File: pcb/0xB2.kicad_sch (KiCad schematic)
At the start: 40 parts, among them J1 USB_C_Receptacle_USB2.0, J2 Conn_01x12, J3 Conn_01x05, J4 Conn_01x12, J5 Conn_01x01, SW1 SW_Push, SW2 SW_Push, U1 RP2040, U2 W25Q32JVZP, U3 XC6210B332MR-G, Y1 Crystal_GND24

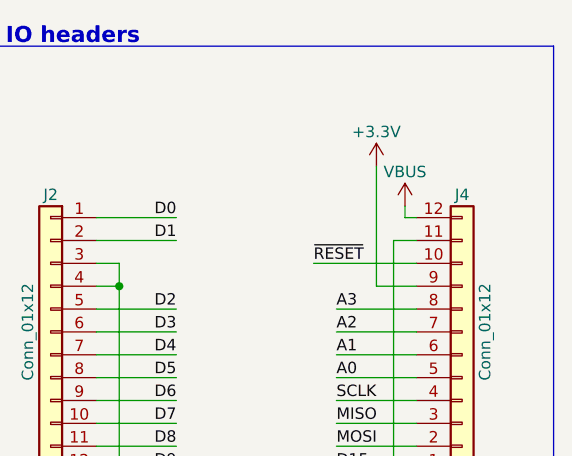
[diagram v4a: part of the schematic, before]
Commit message: Break out 5V instead of VBUS + routing update
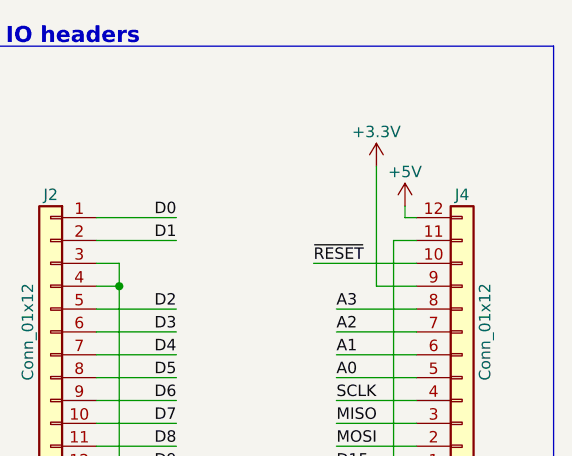
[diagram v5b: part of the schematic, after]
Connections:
- net +5V: now also J4.12 (Pin_12)
- net VBUS: no longer J4.12 (Pin_12)
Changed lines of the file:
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@@
+    (pin "1")
+  )
+  (symbol (lib_id "power:+5V") (at 262.89 38.1 0) (unit 1)
+    (in_bom yes) (on_board yes)
+    (property "Reference" "#PWR?" (id 0) (at 262.89 41.91 0)
+      (effects (font (size 1.27 1.27)) hide)
+    )
+    (property "Value" "+5V" (id 1) (at 262.89 34.29 0))
+    (property "Footprint" "" (id 2) (at 262.89 38.1 0)
+      (effects (font (size 1.27 1.27)) hide)
+    )
+    (property "Datasheet" "" (id 3) (at 262.89 38.1 0)
+      (effects (font (size 1.27 1.27)) hide)
+    )
     (pin "1")
   )
@@
     (pin "1")
   )
-  (symbol (lib_id "power:VBUS") (at 262.89 38.1 0) (unit 1)
-    (in_bom yes) (on_board yes)
-    (property "Reference" "#PWR031" (id 0) (at 262.89 41.91 0)
-      (effects (font (size 1.27 1.27)) hide)
-    )
-    (property "Value" "VBUS" (id 1) (at 262.89 34.29 0))
-    (property "Footprint" "" (id 2) (at 262.89 38.1 0)
-      (effects (font (size 1.27 1.27)) hide)
-    )
-    (property "Datasheet" "" (id 3) (at 262.89 38.1 0)
-      (effects (font (size 1.27 1.27)) hide)
-    )
-    (pin "1")
-  )
   (symbol (lib_id "Device:Polyfuse") (at 59.69 36.83 90) (unit 1)
     (in_bom yes) (on_board yes)
@@
       (reference "#PWR030") (unit 1) (value "GND") (footprint "")
     )
-    (path "/ce7cdfc2-6554-4575-a356-645785e89b5b"
-      (reference "#PWR031") (unit 1) (value "VBUS") (footprint "")
-    )
     (path "/da1644f7-6b59-4f28-b4bd-963f2f055bce"
       (reference "#PWR0101") (unit 1) (value "GND") (footprint "")
@@
       (reference "#PWR0102") (unit 1) (value "VBUS") (footprint "")
     )
+    (path "/0f2f533c-6efa-4396-afac-bd28ecf14786"
+      (reference "#PWR?") (unit 1) (value "+5V") (footprint "")
+    )
     (path "/4a21e78b-0ab0-4b88-8132-9b174e045719"

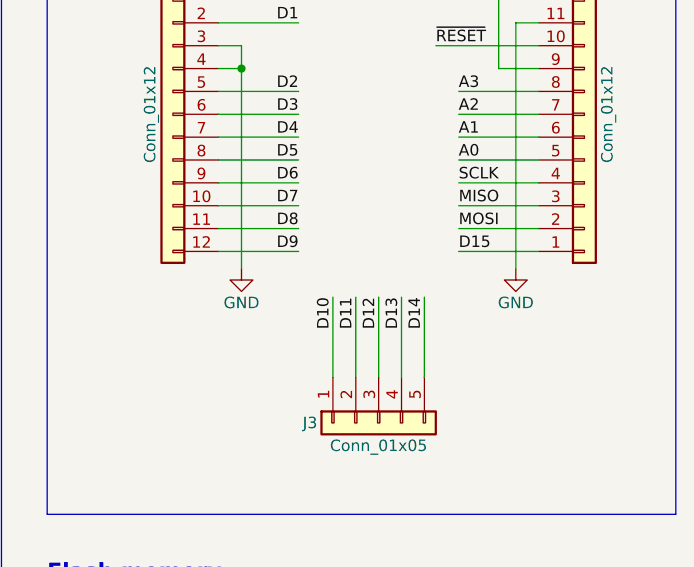
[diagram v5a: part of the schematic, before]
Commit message: Make the pinout compatible with KB2040
WARNING !!! Breaks the compatibility with v1
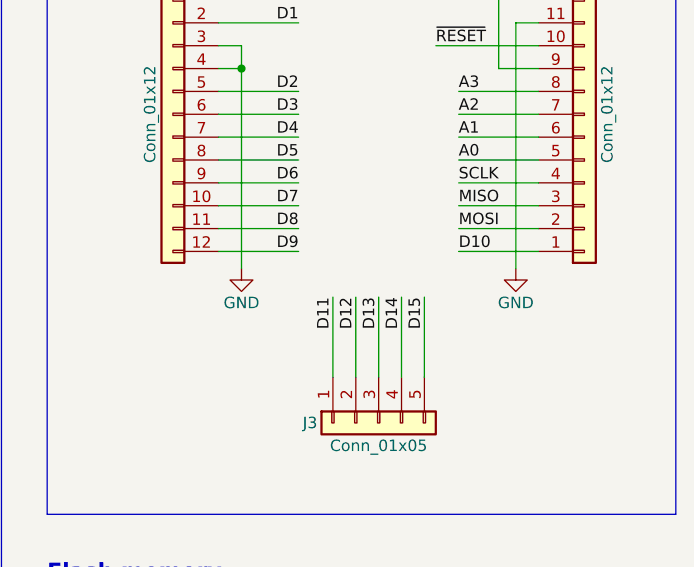
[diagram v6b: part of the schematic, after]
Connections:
- net D10: now also J4.1 (Pin_1); no longer J3.1 (Pin_1)
- net D11: now also J3.1 (Pin_1); no longer J3.2 (Pin_2)
- net D12: now also J3.2 (Pin_2); no longer J3.3 (Pin_3)
- net D13: now also J3.3 (Pin_3); no longer J3.4 (Pin_4)
- net D14: now also J3.4 (Pin_4); no longer J3.5 (Pin_5)
- net D15: now also J3.5 (Pin_5); no longer J4.1 (Pin_1)

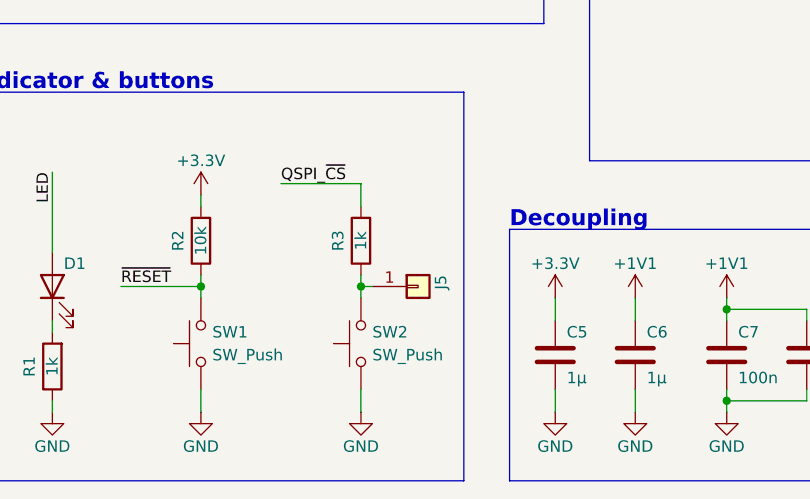
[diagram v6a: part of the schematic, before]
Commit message: Minor routing changes
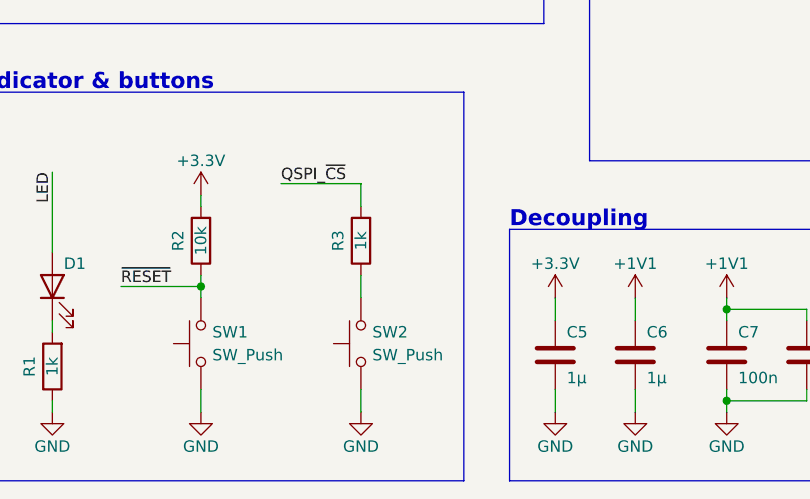
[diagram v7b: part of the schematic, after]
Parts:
- removed J5: Conn_01x01, TestPoint:TestPoint_Pad_D1.0mm, symbol Connector_Generic:Conn_01x01
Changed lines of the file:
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@@
   (junction (at 71.12 44.45) (diameter 0) (color 0 0 0 0)
-  )
-  (junction (at 60.96 172.72) (diameter 0) (color 0 0 0 0)
   )
   (junction (at 130.81 185.42) (diameter 0) (color 0 0 0 0)
@@
     (stroke (width 0) (type default) (color 0 0 0 0))
   )
-  (wire (pts (xy 60.96 171.45) (xy 60.96 172.72))
+  (wire (pts (xy 60.96 171.45) (xy 60.96 173.99))
     (stroke (width 0) (type default) (color 0 0 0 0))
   )
@@
     (stroke (width 0) (type default) (color 0 0 0 0))
   )
-  (wire (pts (xy 60.96 172.72) (xy 60.96 173.99))
-    (stroke (width 0) (type default) (color 0 0 0 0))
-  )
   (wire (pts (xy 228.6 64.77) (xy 237.49 64.77))
     (stroke (width 0) (type default) (color 0 0 0 0))
@@
   )
   (wire (pts (xy 165.1 40.64) (xy 165.1 38.1))
-    (stroke (width 0) (type default) (color 0 0 0 0))
-  )
-  (wire (pts (xy 60.96 172.72) (xy 62.23 172.72))
     (stroke (width 0) (type default) (color 0 0 0 0))
   )
@@
     (pin "1")
   )
-  (symbol (lib_id "Connector_Generic:Conn_01x01") (at 67.31 172.72 0) (unit 1)
-    (in_bom yes) (on_board yes)
-    (property "Reference" "J5" (id 0) (at 69.85 171.45 90)
-      (effects (font (size 1.27 1.27)) (justify right))
-    )
-    (property "Value" "Conn_01x01" (id 1) (at 66.0401 175.26 90)
-      (effects (font (size 1.27 1.27)) (justify right) hide)
-    )
-    (property "Footprint" "TestPoint:TestPoint_Pad_D1.0mm" (id 2) (at 67.31 172.72 0)
-      (effects (font (size 1.27 1.27)) hide)
-    )
-    (property "Datasheet" "~" (id 3) (at 67.31 172.72 0)
-      (effects (font (size 1.27 1.27)) hide)
-    )
-    (pin "1")
-  )
   (symbol (lib_id "power:GND") (at 261.62 69.215 0) (unit 1)
     (in_bom yes) (on_board yes)
@@
       (reference "J4") (unit 1) (value "Conn_01x12") (footprint "0xLib_Connectors:PinHeader_1x12_P2.54mm")
     )
-    (path "/bc3a4b7a-f2c8-40bd-ac75-89d3e5ce5d5b"
-      (reference "J5") (unit 1) (value "Conn_01x01") (footprint "TestPoint:TestPoint_Pad_D1.0mm")
-    )
     (path "/81213cff-519c-4fcf-ae25-6fad0fc859bb"

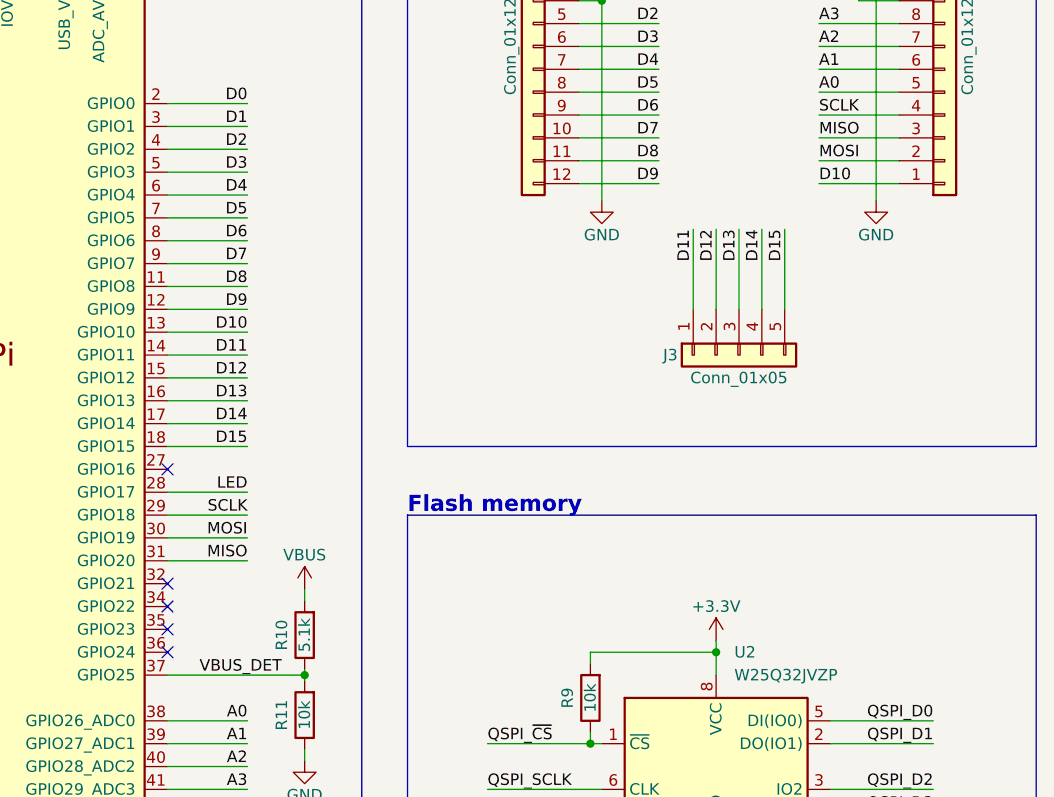
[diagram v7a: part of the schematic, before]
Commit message: Change to Sparkfun RP2040 pinout
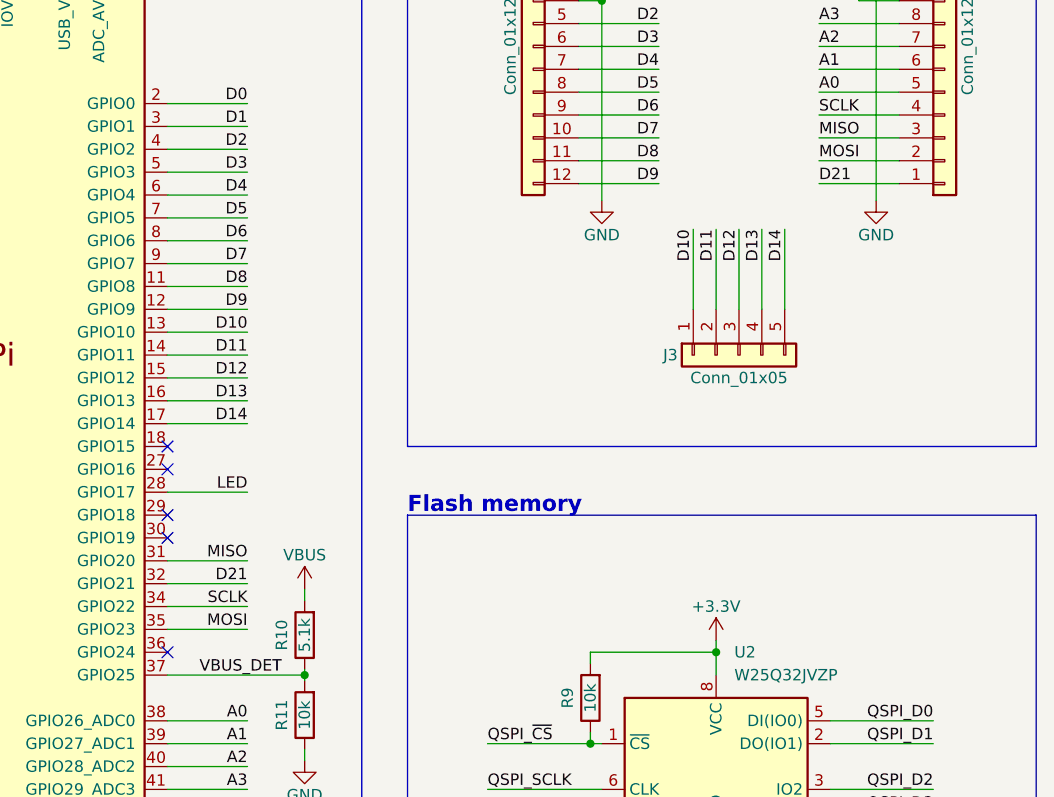
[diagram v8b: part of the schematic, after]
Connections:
- net D10: now also J3.1 (Pin_1); no longer J4.1 (Pin_1)
- net D11: now also J3.2 (Pin_2); no longer J3.1 (Pin_1)
- net D12: now also J3.3 (Pin_3); no longer J3.2 (Pin_2)
- net D13: now also J3.4 (Pin_4); no longer J3.3 (Pin_3)
- net D14: now also J3.5 (Pin_5); no longer J3.4 (Pin_4)
- net MOSI: now also U1.35 (GPIO23); no longer U1.30 (GPIO19)
- net SCLK: now also U1.34 (GPIO22); no longer U1.29 (GPIO18)
- net D21: now reaches U1.32 (GPIO21)
- net D21: now also J4.1 (Pin_1)
- net D15: no longer names the net of U1.18 (GPIO15)
- net D15: no longer J3.5 (Pin_5)
